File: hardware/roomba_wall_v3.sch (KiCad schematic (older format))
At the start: 15 parts, among them CON1 AVR-ISP-6, J2 JSTPH, Q1 Q_NPN_BEC, SW1 Button, SW2 On/Off, U1 ATTINY45-20SU, Y1 8Mhz

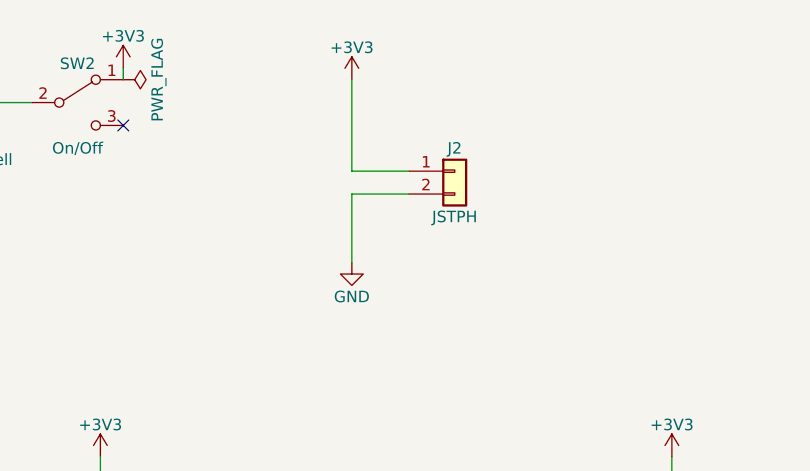
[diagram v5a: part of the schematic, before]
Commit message: Placed and routed new PCB layout
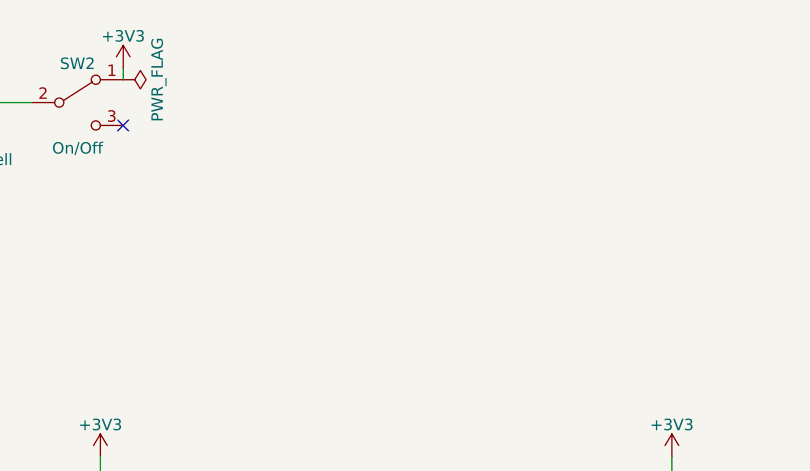
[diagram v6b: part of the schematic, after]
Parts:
- removed J2: JSTPH, lib_fp:JST_PH_B2B-PH-SM4-TB_02x2.00mm_Straight, symbol Conn_01x02
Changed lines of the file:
@@
 Connection ~ 7300 3450
-$Comp
-L Conn_01x02 J2
-U 1 1 5A1C7FC9
-P 8850 1950
-F 0 "J2" H 8850 2050 50  0000 C CNN
-F 1 "JSTPH" H 8850 1750 50  0000 C CNN
-F 2 "lib_fp:JST_PH_B2B-PH-SM4-TB_02x2.00mm_Straight" H 8850 1950 50  0001 C CNN
-F 3 "" H 8850 1950 50  0001 C CNN
-	1    8850 1950
-	1    0    0    -1
-$EndComp
-$Comp
-L +3V3 #PWR010
-U 1 1 5A1C8097
-P 8400 1550
-F 0 "#PWR010" H 8400 1400 50  0001 C CNN
-F 1 "+3V3" H 8400 1690 50  0000 C CNN
-F 2 "" H 8400 1550 50  0001 C CNN
-F 3 "" H 8400 1550 50  0001 C CNN
-	1    8400 1550
-	1    0    0    -1
-$EndComp
-$Comp
-L GND #PWR011
-U 1 1 5A1C86A4
-P 8400 2350
-F 0 "#PWR011" H 8400 2100 50  0001 C CNN
-F 1 "GND" H 8400 2200 50  0000 C CNN
-F 2 "" H 8400 2350 50  0001 C CNN
-F 3 "" H 8400 2350 50  0001 C CNN
-	1    8400 2350
-	1    0    0    -1
-$EndComp
-Wire Wire Line
-	8400 2350 8400 2050
-Wire Wire Line
-	8400 2050 8650 2050
-Wire Wire Line
-	8400 1550 8400 1950
-Wire Wire Line
-	8400 1950 8650 1950
 $Comp
 L Q_NPN_BEC Q1

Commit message: Working on rev B
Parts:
- removed SW2: On/Off, lib_fp:SSSS810701, symbol SW_SPDT
- D2: footprint lib_fp:LED_0603 -> kicad-libs:VSMB3940X01-GS08
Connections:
- net VBAT is gone; now on net +3V3: BT1.1 (+)
- no-connect marks 1 -> 0
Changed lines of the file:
@@
 Sheet 1 1
 Title "Roomba Wall V3"
-Date "2018-03-03"
-Rev "A"
+Date "2018-08-03"
+Rev "B"
 Comp "Petezah"
 Comment1 "(C) 2018 Peter Dunshee"
@@
 F 0 "D2" H 2450 4000 50  0000 C CNN
 F 1 "IR_LED" H 2450 3800 50  0000 C CNN
-F 2 "lib_fp:LED_0603" H 2450 3900 50  0001 C CNN
+F 2 "kicad-libs:VSMB3940X01-GS08" H 2450 3900 50  0001 C CNN
 F 3 "" H 2450 3900 50  0001 C CNN
 	1    2450 3900
@@
 $EndComp
 $Comp
-L VBAT #PWR012
+L VBAT #PWR010
 U 1 1 5A96243B
 P 6400 1500
-F 0 "#PWR012" H 6400 1350 50  0001 C CNN
+F 0 "#PWR010" H 6400 1350 50  0001 C CNN
 F 1 "VBAT" H 6400 1640 50  0000 C CNN
 F 2 "" H 6400 1500 50  0000 C CNN
@@
 	6400 1500 6400 1700
 $Comp
-L GND #PWR013
+L GND #PWR011
 U 1 1 5A962497
 P 6400 2350
-F 0 "#PWR013" H 6400 2100 50  0001 C CNN
+F 0 "#PWR011" H 6400 2100 50  0001 C CNN
 F 1 "GND" H 6400 2200 50  0000 C CNN
 F 2 "" H 6400 2350 50  0001 C CNN
@@
 	1    0    0    -1
 $EndComp
-$Comp
-L SW_SPDT SW2
-U 1 1 5A9625C6
-P 7200 1650
-F 0 "SW2" H 7200 1820 50  0000 C CNN
-F 1 "On/Off" H 7200 1450 50  0000 C CNN
-F 2 "lib_fp:SSSS810701" H 7200 1650 50  0001 C CNN
-F 3 "" H 7200 1650 50  0001 C CNN
-	1    7200 1650
-	1    0    0    -1
-$EndComp
-Wire Wire Line
-	6400 1650 7000 1650
+Wire Wire Line
+	7400 1650 6400 1650
 Connection ~ 6400 1650
 $Comp
-L +3V3 #PWR014
+L +3V3 #PWR012
 U 1 1 5A9626C7
 P 7400 1500
-F 0 "#PWR014" H 7400 1350 50  0001 C CNN
+F 0 "#PWR012" H 7400 1350 50  0001 C CNN
 F 1 "+3V3" H 7400 1640 50  0000 C CNN
 F 2 "" H 7400 1500 50  0001 C CNN
@@
 $EndComp
 Wire Wire Line
-	7400 1500 7400 1550
+	7400 1500 7400 1650
 Wire Wire Line
 	6400 2350 6400 2000
-NoConn ~ 7400 1750
 $Comp
 L SW_Push SW1
@@
 $EndComp
 $Comp
-L GND #PWR015
+L GND #PWR013
 U 1 1 5A962B09
 P 3650 2550
-F 0 "#PWR015" H 3650 2300 50  0001 C CNN
+F 0 "#PWR013" H 3650 2300 50  0001 C CNN
 F 1 "GND" H 3650 2400 50  0000 C CNN
 F 2 "" H 3650 2550 50  0001 C CNN
@@
 SCK/BUTTON
 $Comp
-L +3V3 #PWR016
+L +3V3 #PWR014
 U 1 1 5A962C2C
 P 3650 1550
-F 0 "#PWR016" H 3650 1400 50  0001 C CNN
+F 0 "#PWR014" H 3650 1400 50  0001 C CNN
 F 1 "+3V3" H 3650 1690 50  0000 C CNN
 F 2 "" H 3650 1550 50  0001 C CNN
@@
 	3650 1650 3650 1550
 $Comp
-L PWR_FLAG #FLG017
+L PWR_FLAG #FLG015
 U 1 1 5A9B0C29
 P 6400 2350
-F 0 "#FLG017" H 6400 2425 50  0001 C CNN
+F 0 "#FLG015" H 6400 2425 50  0001 C CNN
 F 1 "PWR_FLAG" H 6400 2500 50  0000 C CNN
 F 2 "" H 6400 2350 50  0001 C CNN
@@
 $EndComp
 $Comp
-L PWR_FLAG #FLG018
+L PWR_FLAG #FLG016
 U 1 1 5A9B0CF1
 P 6400 1500
-F 0 "#FLG018" H 6400 1575 50  0001 C CNN
+F 0 "#FLG016" H 6400 1575 50  0001 C CNN
 F 1 "PWR_FLAG" H 6400 1650 50  0000 C CNN
 F 2 "" H 6400 1500 50  0001 C CNN
@@
 	0    -1   -1   0
 $EndComp
-$Comp
-L PWR_FLAG #FLG019
-U 1 1 5A9B0F1D
-P 7400 1550
-F 0 "#FLG019" H 7400 1625 50  0001 C CNN
-F 1 "PWR_FLAG" H 7400 1700 50  0000 C CNN
-F 2 "" H 7400 1550 50  0001 C CNN
-F 3 "" H 7400 1550 50  0001 C CNN
-	1    7400 1550
-	0    1    1    0
-$EndComp
 $EndSCHEMATC
